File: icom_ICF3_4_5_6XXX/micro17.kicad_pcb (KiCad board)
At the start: 4 copper layers, 20 x 30 mm, 93 parts, among them J1 Conn_01x05, J2 AXK640347YG, J4 USB_B_Micro, U1 STM32G473CCUx, U2 XC6220B331MR, U3 CPC1117N, U4 MCP6002, U5 MCP4451-503-ST, U6 MCP6002, U7 MCP6002, Y1 8 MHz

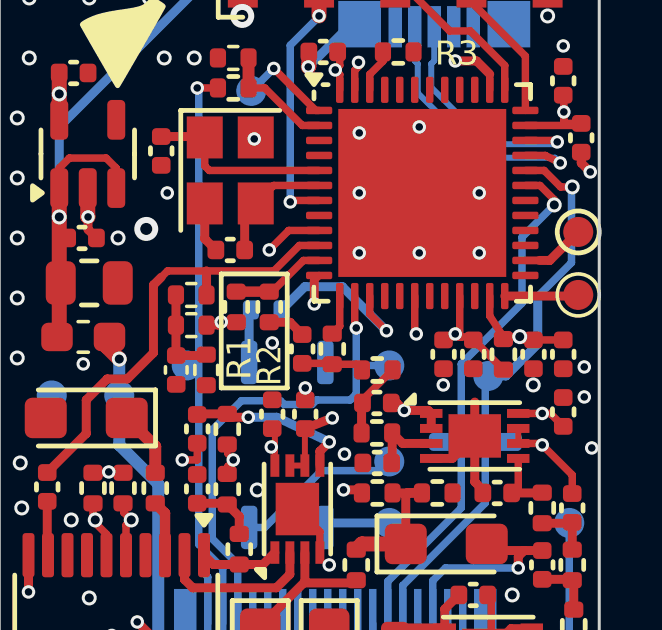
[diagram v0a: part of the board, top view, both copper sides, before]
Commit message: ICOM: fixed floating VREF+ pin
KiCAD version bumped up to 9.0.2
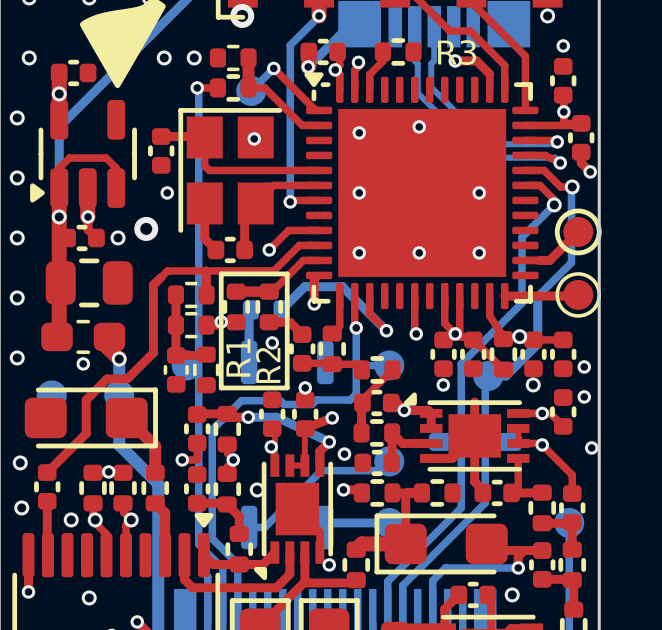
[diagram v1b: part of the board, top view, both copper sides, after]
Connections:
- U1 pad 20: unconnected-(U1-VREF+-Pad20) -> VDDA
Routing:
- net VDDA: track 19.7 -> 21.1 mm

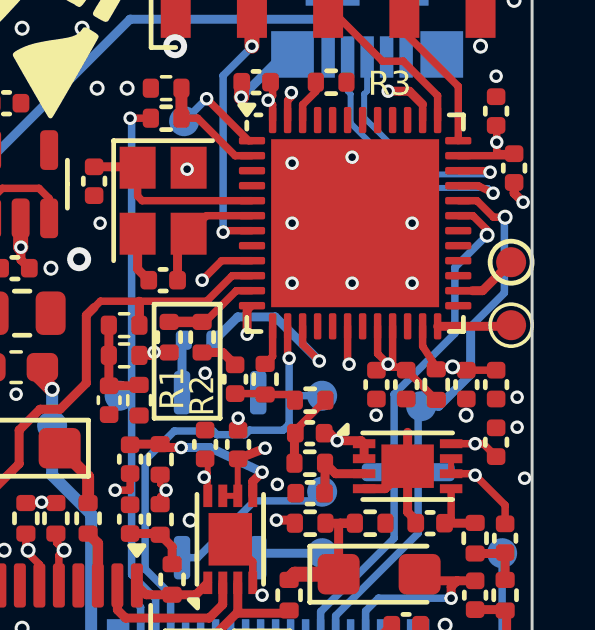
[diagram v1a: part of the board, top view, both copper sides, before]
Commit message: re-routed debug UART
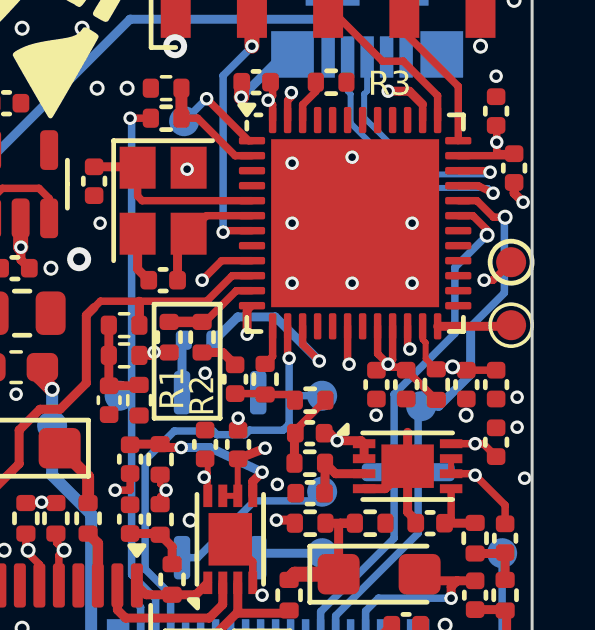
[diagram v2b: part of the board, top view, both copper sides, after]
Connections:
- net USART3_RX renamed Net-(U1-PB11)
- TP12 pad 1: Net-(U1-PB13) -> Net-(U1-PB10)
- U1 pad 22: USART3_TX -> Net-(U1-PB10)
- U1 pad 26: Net-(U1-PB13) -> unconnected-(U1-PB13-Pad26)
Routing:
- net Net-(U1-PB10): track 0.00 -> 5.36 mm, vias 0 -> 2
- net Net-(U1-PB13): track 2.16 -> 0.00 mm
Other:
- board text added: "SP5WWP ON6RF TA1MD UT-M17_v1.1 2026"
- board text removed: "SP5WWP ON6RF TA1MD UT-M17_v1.0 2024"
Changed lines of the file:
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@@
 	(net 42 "unconnected-(U1-PB0-Pad17)")
 	(net 43 "unconnected-(U1-PB2-Pad19)")
-	(net 44 "USART3_RX")
-	(net 45 "USART3_TX")
+	(net 44 "Net-(U1-PB10)")
+	(net 45 "Net-(U1-PB11)")
 	(net 46 "unconnected-(U1-PB15-Pad28)")
 	(net 47 "unconnected-(U1-PC6-Pad29)")
@@
 	(net 105 "unconnected-(U1-PB14-Pad27)")
 	(net 106 "Net-(C12-Pad1)")
-	(net 107 "Net-(U1-PB13)")
+	(net 107 "unconnected-(U1-PB13-Pad26)")
 	(net 108 "unconnected-(U1-PB12-Pad25)")
 	(net 109 "Net-(U1-VBAT)")
@@
 			(layers "F.Cu" "F.Mask" "F.Paste")
 			(roundrect_rratio 0.25)
-			(net 45 "USART3_TX")
+			(net 44 "Net-(U1-PB10)")
 			(pinfunction "PB10")
 			(pintype "bidirectional")
@@
 			(layers "F.Cu" "F.Mask" "F.Paste")
 			(roundrect_rratio 0.25)
-			(net 44 "USART3_RX")
+			(net 45 "Net-(U1-PB11)")
 			(pinfunction "PB11")
 			(pintype "bidirectional")
@@
 			(layers "F.Cu" "F.Mask" "F.Paste")
 			(roundrect_rratio 0.25)
-			(net 107 "Net-(U1-PB13)")
+			(net 107 "unconnected-(U1-PB13-Pad26)")
 			(pinfunction "PB13")
-			(pintype "bidirectional")
+			(pintype "bidirectional+no_connect")
 		)
 		(pad "27" smd roundrect
@@
 			(size 1 1)
 			(layers "F.Cu" "F.Mask")
-			(net 44 "USART3_RX")
+			(net 45 "Net-(U1-PB11)")
 			(pinfunction "1")
 			(pintype "passive")
@@
 			(size 1 1)
 			(layers "F.Cu" "F.Mask")
-			(net 107 "Net-(U1-PB13)")
+			(net 44 "Net-(U1-PB10)")
 			(pinfunction "1")
 			(pintype "passive")
@@
 		)
 	)
-	(gr_text "SP5WWP\nON6RF\nTA1MD\nUT-M17_v1.0\n2024"
+	(gr_text "SP5WWP\nON6RF\nTA1MD\nUT-M17_v1.1\n2026"
 		(at 185.6 59.4 0)
 		(layer "B.SilkS")
@@
 	)
 	(segment
+		(start 196.35 62.9375)
+		(end 196.35 63.376765)
+		(width 0.2)
+		(layer "F.Cu")
+		(net 4)
+	)
+	(segment
 		(start 183.5725 68.8275)
 		(end 183.6 68.8)
@@
 	)
 	(segment
+		(start 196.450358 64.015358)
+		(end 196.805 64.37)
+		(width 0.2)
+		(layer "F.Cu")
+		(net 4)
+	)
+	(segment
+		(start 196.450358 63.477123)
+		(end 196.450358 64.015358)
+		(width 0.2)
+		(layer "F.Cu")
+		(net 4)
+	)
+	(segment
 		(start 197.35 64.29)
 		(end 197.46 64.4)
@@
 	)
 	(segment
-		(start 196.35 63.6)
-		(end 196.8 64.29)
-		(width 0.25)
-		(layer "F.Cu")
-		(net 4)
-	)
-	(segment
 		(start 198.82 57.13)
 		(end 198.82 56.3)
@@
 	)
 	(segment
+		(start 196.35 63.376765)
+		(end 196.450358 63.477123)
+		(width 0.2)
+		(layer "F.Cu")
+		(net 4)
+	)
+	(segment
 		(start 183.75 74.25)
 		(end 184.875 75.375)
@@
 	)
 	(segment
-		(start 196.35 62.9375)
-		(end 196.35 63.6)
-		(width 0.25)
-		(layer "F.Cu")
-		(net 4)
-	)
-	(segment
 		(start 191.35 55.25)
 		(end 191.2 55.4)
@@
 	)
 	(segment
-		(start 194.85 63.85)
+		(start 195.35 64.05)
 		(end 195.2 64.2)
 		(width 0.25)
@@
 	)
 	(segment
-		(start 195.35 64.25)
-		(end 195.4 64.3)
+		(start 194.85 62.9375)
+		(end 194.85 63.85)
 		(width 0.25)
 		(layer "F.Cu")
@@
 	)
 	(segment
-		(start 195.1 64.3)
-		(end 195.2 64.2)
+		(start 195.35 64.25)
+		(end 195.4 64.3)
 		(width 0.25)
 		(layer "F.Cu")
@@
 	)
 	(segment
-		(start 194.85 62.9375)
-		(end 194.85 63.85)
+		(start 195.1 64.3)
+		(end 195.2 64.2)
 		(width 0.25)
 		(layer "F.Cu")
@@
 	)
 	(segment
-		(start 195.35 62.9375)
-		(end 195.35 64.25)
+		(start 194.85 63.85)
+		(end 195.2 64.2)
 		(width 0.25)
 		(layer "F.Cu")
@@
 		(net 5)
 	)
+	(segment
+		(start 195.35 62.9375)
+		(end 195.35 64.05)
+		(width 0.25)
+		(layer "F.Cu")
+		(net 5)
+	)
 	(via
 		(at 195.2 64.2)
@@
 	)
 	(segment
+		(start 195.85 62.9375)
+		(end 195.85 63.620642)
+		(width 0.25)
+		(layer "F.Cu")
+		(net 44)
+	)
+	(segment
+		(start 198.7 61.4)
+		(end 199.3 60.8)
+		(width 0.25)
+		(layer "F.Cu")
+		(net 44)
+	)
+	(segment
+		(start 198.4 61.4)
+		(end 198.7 61.4)
+		(width 0.25)
+		(layer "F.Cu")
+		(net 44)
+	)
+	(segment
+		(start 195.85 63.620642)
+		(end 195.924358 63.695)
+		(width 0.25)
+		(layer "F.Cu")
+		(net 44)
+	)
+	(via
+		(at 195.924358 63.695)
+		(size 0.45)
+		(drill 0.25)
+		(layers "F.Cu" "B.Cu")
+		(net 44)
+	)
+	(via
+		(at 198.4 61.4)
+		(size 0.45)
+		(drill 0.25)
+		(layers "F.Cu" "B.Cu")
+		(net 44)
+	)
+	(segment
+		(start 196.105 63.695)
+		(end 198.4 61.4)
+		(width 0.25)
+		(layer "In2.Cu")
+		(net 44)
+	)
+	(segment
+		(start 195.924358 63.695)
+		(end 196.105 63.695)
+		(width 0.25)
+		(layer "In2.Cu")
+		(net 44)
+	)
+	(segment
 		(start 196.85 62.9375)
 		(end 199.2625 62.9375)
 		(width 0.3)
 		(layer "F.Cu")
-		(net 44)
+		(net 45)
 	)
 	(segment
@@
 		(width 0.3)
 		(layer "F.Cu")
-		(net 44)
+		(net 45)
 	)
 	(segment
@@
 	)
 	(segment
-		(start 197.5375 61.75)
-		(end 198 61.75)
-		(width 0.25)
-		(layer "F.Cu")
-		(net 107)
-	)
-	(segment
-		(start 198.35 61.75)
-		(end 199.3 60.8)
-		(width 0.3)
-		(layer "F.Cu")
-		(net 107)
-	)
-	(segment
-		(start 198 61.75)
-		(end 198.35 61.75)
-		(width 0.3)
-		(layer "F.Cu")
-		(net 107)
-	)
-	(segment
